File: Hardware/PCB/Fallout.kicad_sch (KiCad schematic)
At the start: 82 parts, among them J1 USB_A, J2 USB_C_Receptacle_USB2.0_14P, J3 Conn_01x16, Q1 P-Channel MOSFET, Q10 2N3906, Q11 P-Channel MOSFET, Q12 2N3904, Q13 2N3904, Q14 2N3904, Q15 P-Channel MOSFET, Q16 2N3904, Q17 2N3904, Q18 P-Channel MOSFET, Q19 2N3904, Q2 2N3904, Q20 2N3904, Q21 2N3904, Q22 P-Channel MOSFET, Q23 2N3904, Q3 2N3904, Q4 P-Channel MOSFET, Q5 2N3906, Q6 2N3904, Q7 2N3906, Q8 P-Channel MOSFET, Q9 2N3904, SW1 SW_Push, SW2 SW_Push, SW3 SW_Push, SW4 SW_Push, SW5 SW_Push, SW6 SW_Push, SW7 SW_Push, SW8 SW_Push, SW9 SW_Push, U1 ESP32-S3-WROOM-1, U2 AMS1117-3.3

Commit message: Schematic Final
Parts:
- removed C1: 0.1uf, Capacitor_THT:C_Disc_D5.0mm_W2.5mm_P2.50mm., symbol Device:C
- removed C2: 10.0uf, Capacitor_THT:C_Disc_D5.0mm_W2.5mm_P2.50mm, symbol Device:C
- removed MES1: Voltmeter_DC, symbol Device:Voltmeter_DC
- removed Q1, Q11, Q15, Q18, Q22, Q4, Q8: P-Channel MOSFET, Package_TO_SOT_THT:TO-220-3_Vertical, symbol Transistor_FET:IRF9540N
- removed Q10, Q5, Q7: 2N3906, Package_TO_SOT_THT:TO-92_Inline, symbol Transistor_BJT:2N3906
- removed Q12, Q13, Q14, Q16, Q17, Q19, Q2, Q20, Q21, Q23, Q3, Q6, Q9: 2N3904, Package_TO_SOT_THT:TO-92_Inline, symbol Transistor_BJT:2N3904
- removed R1, R2: 4.7k, symbol Device:R
- removed R10, R11, R20, R22, R24, R25, R26, R28, R29, R30, R31, R33, R34, R35, R36, R37, R38, R39, R40, R5, R6, R7: 10k, symbol Device:R
- removed R12, R15, R16, R21, R23, R27, R32, R8, R9: 1k~10k, symbol Device:R
- removed R13: 3.3k, symbol Device:R
- removed R14: 1.7k, symbol Device:R
- removed R17: 3.3, symbol Device:R
- removed R18: 1.7, symbol Device:R
- removed R19: 5k, symbol Device:R
- removed SW1, SW2, SW3, SW4, SW5, SW6, SW7, SW8, SW9: SW_Push, symbol Switch:SW_Push
- removed U2: AMS1117-3.3, Package_TO_SOT_SMD:SOT-223-3_TabPin2, symbol Regulator_Linear:AMS1117-3.3
- added Q24, Q25, Q26, Q27: 2N3904, Package_TO_SOT_THT:TO-92_Inline, symbol Transistor_BJT:2N3904
- added Q28: P-Channel MOSFET, Package_TO_SOT_THT:TO-220-3_Vertical, symbol Transistor_FET:IRF9540N
- added R41, R42, R43, R44, R45, R46: 10k, symbol Device:R
- added SW10: SW_Push, symbol Switch:SW_Push
- C3: value 10uf -> 0.1uf; footprint (none) -> Capacitor_THT:C_Disc_D5.0mm_W2.5mm_P2.50mm.
- C4: value 10uf -> 10.0uf; footprint (none) -> Capacitor_THT:C_Disc_D5.0mm_W2.5mm_P2.50mm
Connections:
- net D+: no longer J2.A6 (D+), J2.B6 (D+)
- net D-: no longer J2.A7 (D-), J2.B7 (D-)
- net GND: now also C3.2, Q24.1 (E), Q25.1 (E), Q27.1 (E), SW10.1; no longer C3.1, U1.1 (GND), U1.40 (GND), U1.41 (GND)
- net POWER: now also R41.2, R42.1
- net PWR_SIG: now also Q27.3 (C)
- net VBUS: now also Q28.3 (S), R43.1, R45.2, R46.2
- net VCC: now also C3.1; no longer U1.2 (3V3)
- net VIN: now also Q28.2 (D); no longer C3.2
- new net: U1.1 (GND), U1.40 (GND), U1.41 (GND)
- new net: Q26.1 (E), R44.1, R45.1, SW10.2
- new net: Q24.3 (C), Q26.2 (B), R43.2
- new net: Q25.3 (C), Q26.3 (C), Q28.1 (G), R46.1
- new net: Q27.2 (B), R44.2
- new net: Q24.2 (B), R41.1
- new net: Q25.2 (B), R42.2
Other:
- note added: "ESP32"
- note added: "USB-A Receptacle"
- note added: "USB-C Receptacle"
- note added: "VBUS is the raw output from the USB-C VIN is the 5V input to the devboard VCC is the 3V3 output from the devboard"
- note added: "VCC is the 3v3 output frome the devboard GND is the ground pin of the devboard 3v3 and GND not connected here because this diagram is the raw chip but not the devboard that is used in this project"
- note removed: "Boot"
- note removed: "Decoupling Capacitors"
- note removed: "Linear Regulator"
- note removed: "Pull up"
- note removed: "USB Receptacle"
- note removed: "USB-A Input"
- note removed: "VBUS is the raw input from the USB-C VIN is the 5V input VCC is the 3V3 input"
- moved on the sheet: J1, J2, J3, R3, R4

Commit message: Create PowerButton PCB
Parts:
- removed C3: 0.1uf, Capacitor_THT:C_Disc_D5.0mm_W2.5mm_P2.50mm., symbol Device:C
- added C5: 0.1uf, Capacitor_THT:C_Disc_D5.0mm_W2.5mm_P2.50mm, symbol Device:C
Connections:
- net GND: now also U1.1 (GND), U1.40 (GND), U1.41 (GND), C5.2
- net VBUS: now also J1.1 (VBUS)
- net VCC: now also C5.1
- net VIN: now also U1.2 (3V3)
- net EN: no longer names the net of U1.3 (EN)
- net IO0: no longer names the net of U1.27 (IO0)
- no-connect marks 0 -> 26
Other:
- moved on the sheet: J1, J2, R3, R4

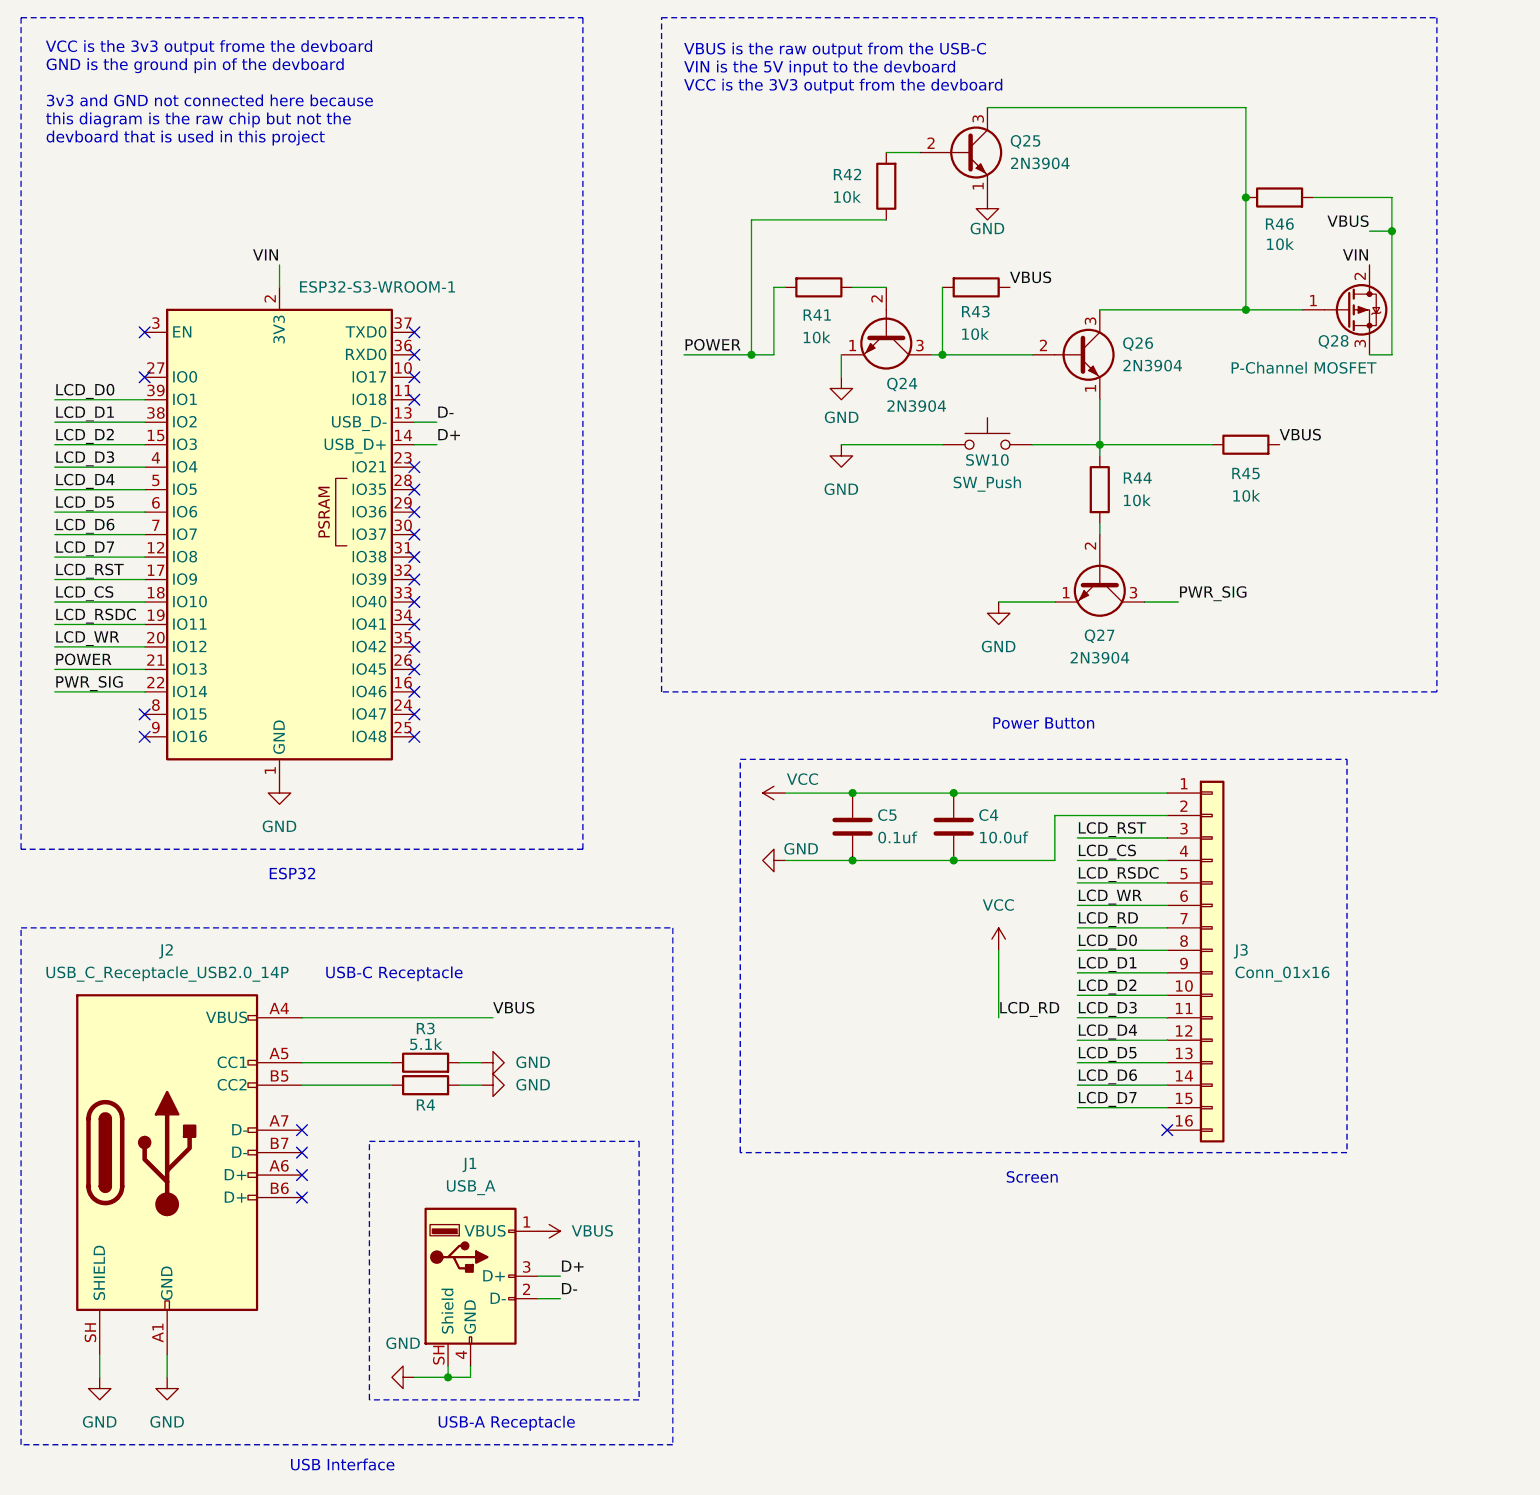
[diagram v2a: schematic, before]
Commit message: Push before system switch - my arch crashed, have tgo switch to windows now
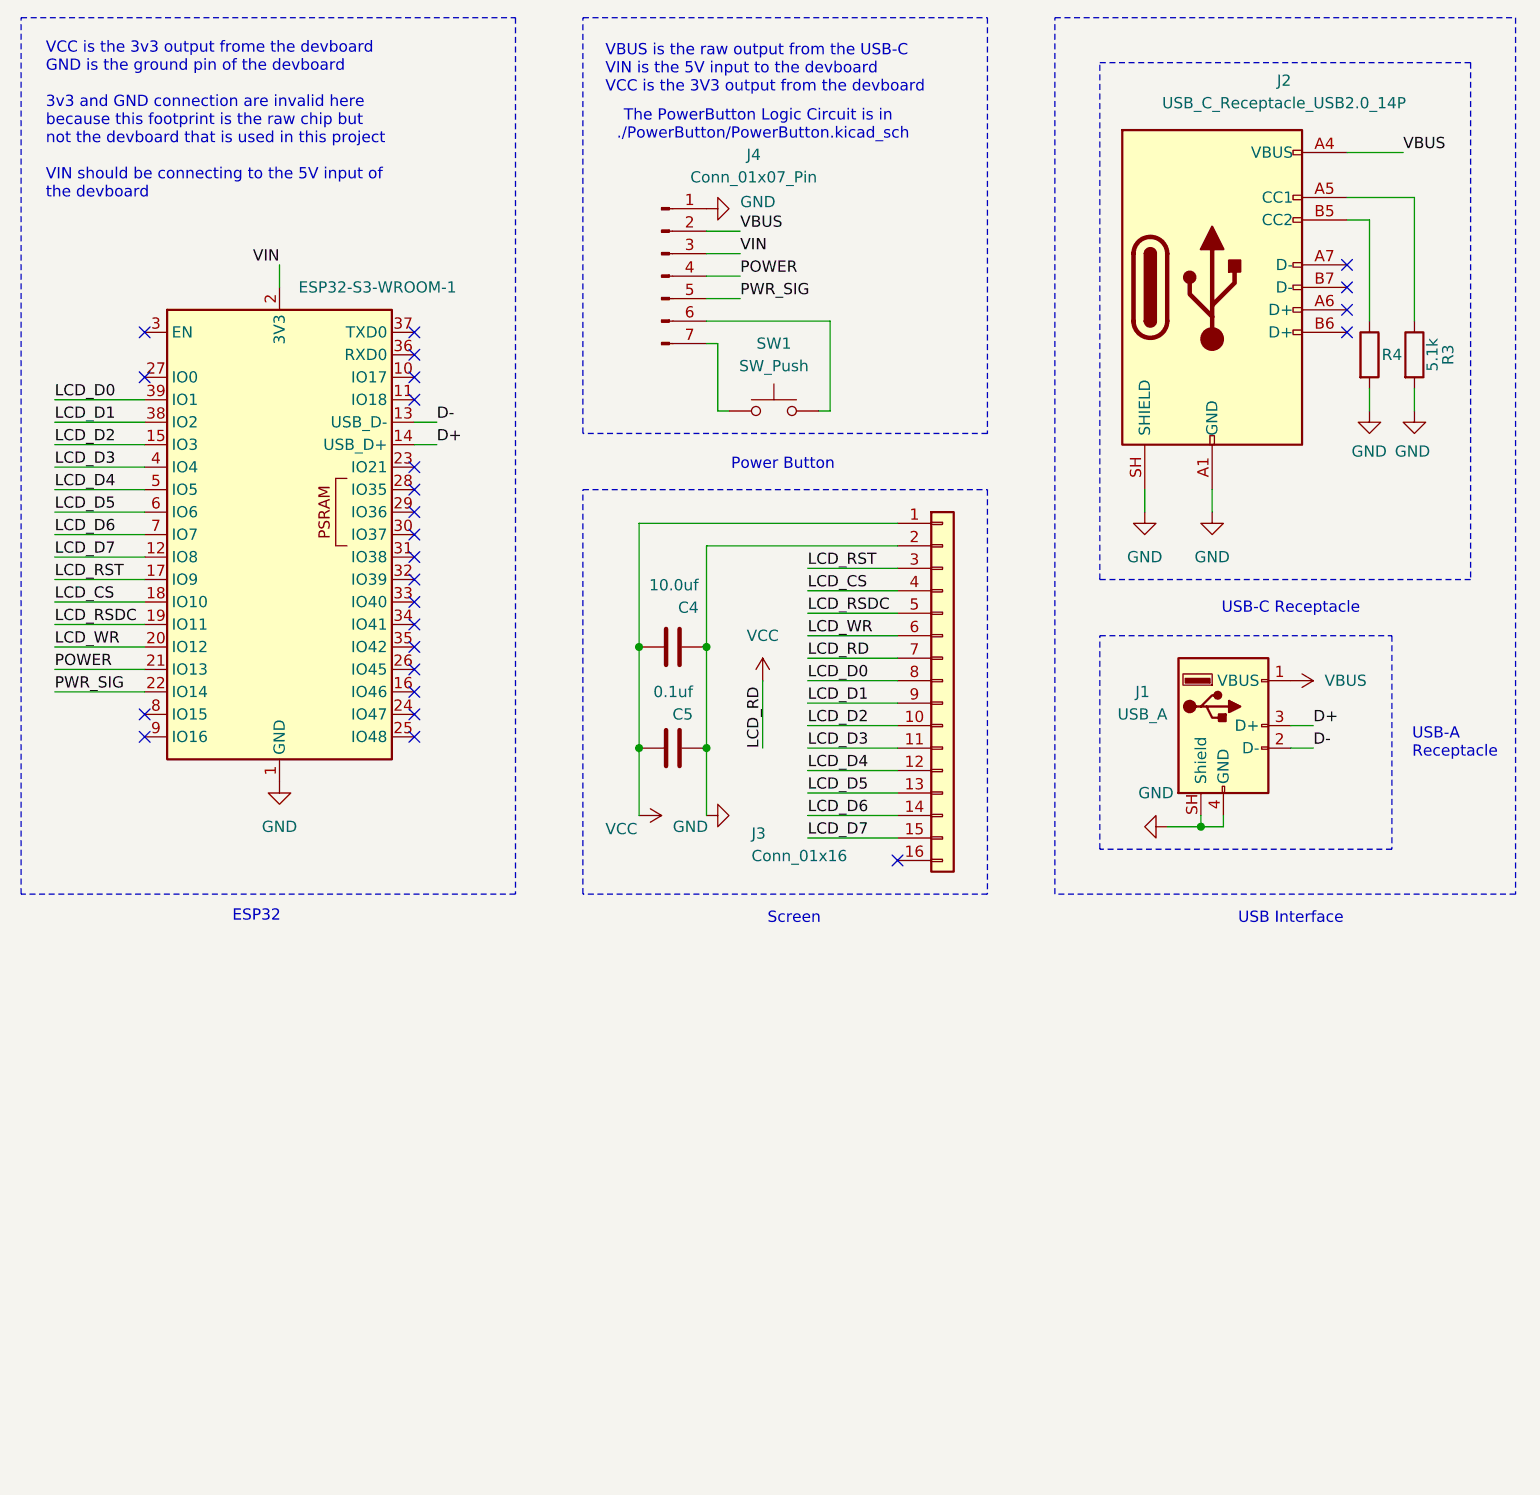
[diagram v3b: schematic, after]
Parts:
- removed Q24, Q25, Q26, Q27: 2N3904, Package_TO_SOT_THT:TO-92_Inline, symbol Transistor_BJT:2N3904
- removed Q28: P-Channel MOSFET, Package_TO_SOT_THT:TO-220-3_Vertical, symbol Transistor_FET:IRF9540N
- removed R41, R42, R43, R44, R45, R46: 10k, symbol Device:R
- removed SW10: SW_Push, symbol Switch:SW_Push
- added J4: Conn_01x07_Pin, symbol Connector:Conn_01x07_Pin
- added SW1: SW_Push, symbol Switch:SW_Push
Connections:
- net GND: now also J4.1 (Pin_1)
- net POWER: now also J4.4 (Pin_4)
- net PWR_SIG: now also J4.5 (Pin_5)
- net VBUS: now also J4.2 (Pin_2)
- net VIN: now also J4.3 (Pin_3)
- new net: J4.6 (Pin_6), SW1.2
- new net: J4.7 (Pin_7), SW1.1
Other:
- note added: "The PowerButton Logic Circuit is in ./PowerButton/PowerButton.kicad_sch"
- note added: "VCC is the 3v3 output frome the devboard GND is the ground pin of the devboard 3v3 and GND connection are invalid here because this footprint is the raw chip but not the devboard that is used in this project VIN should be connecting to the 5V input of the devboard"
- note removed: "VCC is the 3v3 output frome the devboard GND is the ground pin of the devboard 3v3 and GND not connected here because this diagram is the raw chip but not the devboard that is used in this project"
- moved on the sheet: C4, C5, J1, J2, J3, R3, R4
